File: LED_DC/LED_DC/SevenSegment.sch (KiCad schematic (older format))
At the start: 15 parts

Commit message: Removed redundant files
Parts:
- gave numbers to parts that had none: 15
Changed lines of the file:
@@
 $EndDescr
 $Comp
-L Display_Character:KCSA02-136 U?
+L Display_Character:KCSA02-136 U9
 U 1 1 5FB55AD1
 P 7650 2000
-F 0 "U?" H 7650 2667 50  0000 C CNN
+F 0 "U9" H 7650 2667 50  0000 C CNN
 F 1 "KCSA02-136" H 7650 2576 50  0000 C CNN
 F 2 "Display_7Segment:KCSC02-136" H 7650 1400 50  0001 C CNN
@@
 DP
 $Comp
-L Display_Character:KCSA02-136 U?
+L Display_Character:KCSA02-136 U3
 U 1 1 5FB5CA24
 P 1200 2000
-F 0 "U?" H 1200 2667 50  0000 C CNN
+F 0 "U3" H 1200 2667 50  0000 C CNN
 F 1 "KCSA02-136" H 1200 2576 50  0000 C CNN
 F 2 "Display_7Segment:KCSC02-136" H 1200 1400 50  0001 C CNN
@@
 DP
 $Comp
-L Display_Character:KCSA02-136 U?
+L Display_Character:KCSA02-136 U4
 U 1 1 5FB5E544
 P 2450 2000
-F 0 "U?" H 2450 2667 50  0000 C CNN
+F 0 "U4" H 2450 2667 50  0000 C CNN
 F 1 "KCSA02-136" H 2450 2576 50  0000 C CNN
 F 2 "Display_7Segment:KCSC02-136" H 2450 1400 50  0001 C CNN
@@
 DP
 $Comp
-L Display_Character:KCSA02-136 U?
+L Display_Character:KCSA02-136 U5
 U 1 1 5FB5F30B
 P 3550 2000
-F 0 "U?" H 3550 2667 50  0000 C CNN
+F 0 "U5" H 3550 2667 50  0000 C CNN
 F 1 "KCSA02-136" H 3550 2576 50  0000 C CNN
 F 2 "Display_7Segment:KCSC02-136" H 3550 1400 50  0001 C CNN
@@
 DP
 $Comp
-L Display_Character:KCSA02-136 U?
+L Display_Character:KCSA02-136 U6
 U 1 1 5FB6054A
 P 4550 2000
-F 0 "U?" H 4550 2667 50  0000 C CNN
+F 0 "U6" H 4550 2667 50  0000 C CNN
 F 1 "KCSA02-136" H 4550 2576 50  0000 C CNN
 F 2 "Display_7Segment:KCSC02-136" H 4550 1400 50  0001 C CNN
@@
 DP
 $Comp
-L Display_Character:KCSA02-136 U?
+L Display_Character:KCSA02-136 U7
 U 1 1 5FB633C5
 P 5550 2000
-F 0 "U?" H 5550 2667 50  0000 C CNN
+F 0 "U7" H 5550 2667 50  0000 C CNN
 F 1 "KCSA02-136" H 5550 2576 50  0000 C CNN
 F 2 "Display_7Segment:KCSC02-136" H 5550 1400 50  0001 C CNN
@@
 DP
 $Comp
-L Display_Character:KCSA02-136 U?
+L Display_Character:KCSA02-136 U8
 U 1 1 5FB65C47
 P 6550 2000
-F 0 "U?" H 6550 2667 50  0000 C CNN
+F 0 "U8" H 6550 2667 50  0000 C CNN
 F 1 "KCSA02-136" H 6550 2576 50  0000 C CNN
 F 2 "Display_7Segment:KCSC02-136" H 6550 1400 50  0001 C CNN
@@
 DP
 $Comp
-L Device:LED D?
+L Device:LED D2
 U 1 1 5FAF58A5
 P 4750 4800
-F 0 "D?" H 4743 5017 50  0000 C CNN
+F 0 "D2" H 4743 5017 50  0000 C CNN
 F 1 "LED" H 4743 4926 50  0000 C CNN
 F 2 "" H 4750 4800 50  0001 C CNN
@@
 $EndComp
 $Comp
-L Device:LED D?
+L Device:LED D5
 U 1 1 5FAF841D
 P 5850 4350
-F 0 "D?" H 5843 4567 50  0000 C CNN
+F 0 "D5" H 5843 4567 50  0000 C CNN
 F 1 "LED" H 5843 4476 50  0000 C CNN
 F 2 "" H 5850 4350 50  0001 C CNN
@@
 $EndComp
 $Comp
-L Device:LED D?
+L Device:LED D1
 U 1 1 5FAFB32B
 P 4750 4450
-F 0 "D?" H 4743 4667 50  0000 C CNN
+F 0 "D1" H 4743 4667 50  0000 C CNN
 F 1 "LED" H 4743 4576 50  0000 C CNN
 F 2 "" H 4750 4450 50  0001 C CNN
@@
 $EndComp
 $Comp
-L Device:LED D?
+L Device:LED D3
 U 1 1 5FAFBFC1
 P 4750 5150
-F 0 "D?" H 4743 5367 50  0000 C CNN
+F 0 "D3" H 4743 5367 50  0000 C CNN
 F 1 "LED" H 4743 5276 50  0000 C CNN
 F 2 "" H 4750 5150 50  0001 C CNN
@@
 $EndComp
 $Comp
-L Device:LED D?
+L Device:LED D4
 U 1 1 5FAFC42C
 P 4750 5500
-F 0 "D?" H 4743 5717 50  0000 C CNN
+F 0 "D4" H 4743 5717 50  0000 C CNN
 F 1 "LED" H 4743 5626 50  0000 C CNN
 F 2 "" H 4750 5500 50  0001 C CNN
@@
 $EndComp
 $Comp
-L Device:LED D?
+L Device:LED D6
 U 1 1 5FAFC938
 P 5850 4750
-F 0 "D?" H 5843 4967 50  0000 C CNN
+F 0 "D6" H 5843 4967 50  0000 C CNN
 F 1 "LED" H 5843 4876 50  0000 C CNN
 F 2 "" H 5850 4750 50  0001 C CNN
@@
 $EndComp
 $Comp
-L Device:LED D?
+L Device:LED D7
 U 1 1 5FAFCD00
 P 5850 5100
-F 0 "D?" H 5843 5317 50  0000 C CNN
+F 0 "D7" H 5843 5317 50  0000 C CNN
 F 1 "LED" H 5843 5226 50  0000 C CNN
 F 2 "" H 5850 5100 50  0001 C CNN
@@
 $EndComp
 $Comp
-L Device:LED D?
+L Device:LED D8
 U 1 1 5FAFD0BD
 P 5850 5500
-F 0 "D?" H 5843 5717 50  0000 C CNN
+F 0 "D8" H 5843 5717 50  0000 C CNN
 F 1 "LED" H 5843 5626 50  0000 C CNN
 F 2 "" H 5850 5500 50  0001 C CNN

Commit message: Added foot prints for the components.
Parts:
- D1, D2, D3, D4, D5, D6, D7, D8: footprint (none) -> LED_SMD:LED_0603_1608Metric_Pad1.05x0.95mm_HandSolder
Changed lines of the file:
@@
 F 0 "D2" H 4743 5017 50  0000 C CNN
 F 1 "LED" H 4743 4926 50  0000 C CNN
-F 2 "" H 4750 4800 50  0001 C CNN
+F 2 "LED_SMD:LED_0603_1608Metric_Pad1.05x0.95mm_HandSolder" H 4750 4800 50  0001 C CNN
 F 3 "~" H 4750 4800 50  0001 C CNN
 	1    4750 4800
@@
 F 0 "D5" H 5843 4567 50  0000 C CNN
 F 1 "LED" H 5843 4476 50  0000 C CNN
-F 2 "" H 5850 4350 50  0001 C CNN
+F 2 "LED_SMD:LED_0603_1608Metric_Pad1.05x0.95mm_HandSolder" H 5850 4350 50  0001 C CNN
 F 3 "~" H 5850 4350 50  0001 C CNN
 	1    5850 4350
@@
 F 0 "D1" H 4743 4667 50  0000 C CNN
 F 1 "LED" H 4743 4576 50  0000 C CNN
-F 2 "" H 4750 4450 50  0001 C CNN
+F 2 "LED_SMD:LED_0603_1608Metric_Pad1.05x0.95mm_HandSolder" H 4750 4450 50  0001 C CNN
 F 3 "~" H 4750 4450 50  0001 C CNN
 	1    4750 4450
@@
 F 0 "D3" H 4743 5367 50  0000 C CNN
 F 1 "LED" H 4743 5276 50  0000 C CNN
-F 2 "" H 4750 5150 50  0001 C CNN
+F 2 "LED_SMD:LED_0603_1608Metric_Pad1.05x0.95mm_HandSolder" H 4750 5150 50  0001 C CNN
 F 3 "~" H 4750 5150 50  0001 C CNN
 	1    4750 5150
@@
 F 0 "D4" H 4743 5717 50  0000 C CNN
 F 1 "LED" H 4743 5626 50  0000 C CNN
-F 2 "" H 4750 5500 50  0001 C CNN
+F 2 "LED_SMD:LED_0603_1608Metric_Pad1.05x0.95mm_HandSolder" H 4750 5500 50  0001 C CNN
 F 3 "~" H 4750 5500 50  0001 C CNN
 	1    4750 5500
@@
 F 0 "D6" H 5843 4967 50  0000 C CNN
 F 1 "LED" H 5843 4876 50  0000 C CNN
-F 2 "" H 5850 4750 50  0001 C CNN
+F 2 "LED_SMD:LED_0603_1608Metric_Pad1.05x0.95mm_HandSolder" H 5850 4750 50  0001 C CNN
 F 3 "~" H 5850 4750 50  0001 C CNN
 	1    5850 4750
@@
 F 0 "D7" H 5843 5317 50  0000 C CNN
 F 1 "LED" H 5843 5226 50  0000 C CNN
-F 2 "" H 5850 5100 50  0001 C CNN
+F 2 "LED_SMD:LED_0603_1608Metric_Pad1.05x0.95mm_HandSolder" H 5850 5100 50  0001 C CNN
 F 3 "~" H 5850 5100 50  0001 C CNN
 	1    5850 5100
@@
 F 0 "D8" H 5843 5717 50  0000 C CNN
 F 1 "LED" H 5843 5626 50  0000 C CNN
-F 2 "" H 5850 5500 50  0001 C CNN
+F 2 "LED_SMD:LED_0603_1608Metric_Pad1.05x0.95mm_HandSolder" H 5850 5500 50  0001 C CNN
 F 3 "~" H 5850 5500 50  0001 C CNN
 	1    5850 5500

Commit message: updated the foot print assignment.
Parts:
- U3, U4, U5, U6, U7, U8, U9: footprint Display_7Segment:KCSC02-136 -> Display_7Segment:7SegmentLED_LTS6760_LTS6780
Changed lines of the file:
@@
 F 0 "U9" H 7650 2667 50  0000 C CNN
 F 1 "KCSA02-136" H 7650 2576 50  0000 C CNN
-F 2 "Display_7Segment:KCSC02-136" H 7650 1400 50  0001 C CNN
+F 2 "Display_7Segment:7SegmentLED_LTS6760_LTS6780" H 7650 1400 50  0001 C CNN
 F 3 "http://www.kingbright.com/attachments/file/psearch/000/00/00/KCSA02-136(Ver.7B).pdf" H 7150 2475 50  0001 L CNN
 	1    7650 2000
@@
 F 0 "U3" H 1200 2667 50  0000 C CNN
 F 1 "KCSA02-136" H 1200 2576 50  0000 C CNN
-F 2 "Display_7Segment:KCSC02-136" H 1200 1400 50  0001 C CNN
+F 2 "Display_7Segment:7SegmentLED_LTS6760_LTS6780" H 1200 1400 50  0001 C CNN
 F 3 "http://www.kingbright.com/attachments/file/psearch/000/00/00/KCSA02-136(Ver.7B).pdf" H 700 2475 50  0001 L CNN
 	1    1200 2000
@@
 F 0 "U4" H 2450 2667 50  0000 C CNN
 F 1 "KCSA02-136" H 2450 2576 50  0000 C CNN
-F 2 "Display_7Segment:KCSC02-136" H 2450 1400 50  0001 C CNN
+F 2 "Display_7Segment:7SegmentLED_LTS6760_LTS6780" H 2450 1400 50  0001 C CNN
 F 3 "http://www.kingbright.com/attachments/file/psearch/000/00/00/KCSA02-136(Ver.7B).pdf" H 1950 2475 50  0001 L CNN
 	1    2450 2000
@@
 F 0 "U5" H 3550 2667 50  0000 C CNN
 F 1 "KCSA02-136" H 3550 2576 50  0000 C CNN
-F 2 "Display_7Segment:KCSC02-136" H 3550 1400 50  0001 C CNN
+F 2 "Display_7Segment:7SegmentLED_LTS6760_LTS6780" H 3550 1400 50  0001 C CNN
 F 3 "http://www.kingbright.com/attachments/file/psearch/000/00/00/KCSA02-136(Ver.7B).pdf" H 3050 2475 50  0001 L CNN
 	1    3550 2000
@@
 F 0 "U6" H 4550 2667 50  0000 C CNN
 F 1 "KCSA02-136" H 4550 2576 50  0000 C CNN
-F 2 "Display_7Segment:KCSC02-136" H 4550 1400 50  0001 C CNN
+F 2 "Display_7Segment:7SegmentLED_LTS6760_LTS6780" H 4550 1400 50  0001 C CNN
 F 3 "http://www.kingbright.com/attachments/file/psearch/000/00/00/KCSA02-136(Ver.7B).pdf" H 4050 2475 50  0001 L CNN
 	1    4550 2000
@@
 F 0 "U7" H 5550 2667 50  0000 C CNN
 F 1 "KCSA02-136" H 5550 2576 50  0000 C CNN
-F 2 "Display_7Segment:KCSC02-136" H 5550 1400 50  0001 C CNN
+F 2 "Display_7Segment:7SegmentLED_LTS6760_LTS6780" H 5550 1400 50  0001 C CNN
 F 3 "http://www.kingbright.com/attachments/file/psearch/000/00/00/KCSA02-136(Ver.7B).pdf" H 5050 2475 50  0001 L CNN
 	1    5550 2000
@@
 F 0 "U8" H 6550 2667 50  0000 C CNN
 F 1 "KCSA02-136" H 6550 2576 50  0000 C CNN
-F 2 "Display_7Segment:KCSC02-136" H 6550 1400 50  0001 C CNN
+F 2 "Display_7Segment:7SegmentLED_LTS6760_LTS6780" H 6550 1400 50  0001 C CNN
 F 3 "http://www.kingbright.com/attachments/file/psearch/000/00/00/KCSA02-136(Ver.7B).pdf" H 6050 2475 50  0001 L CNN
 	1    6550 2000

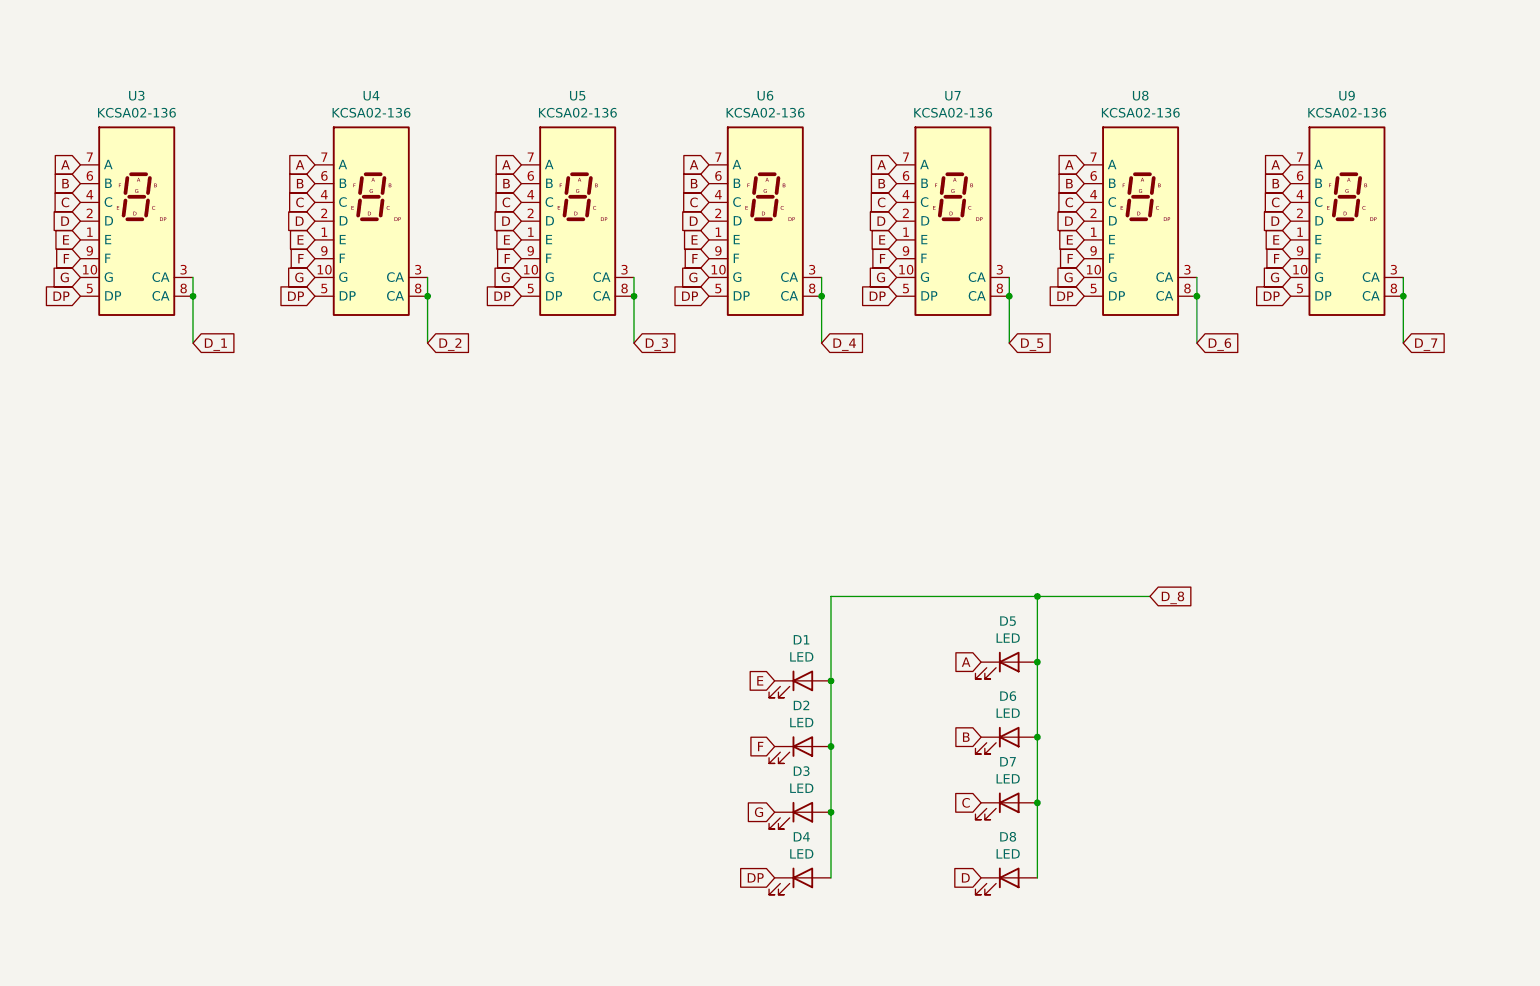
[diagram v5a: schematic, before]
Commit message: Added text to the schematic sections.
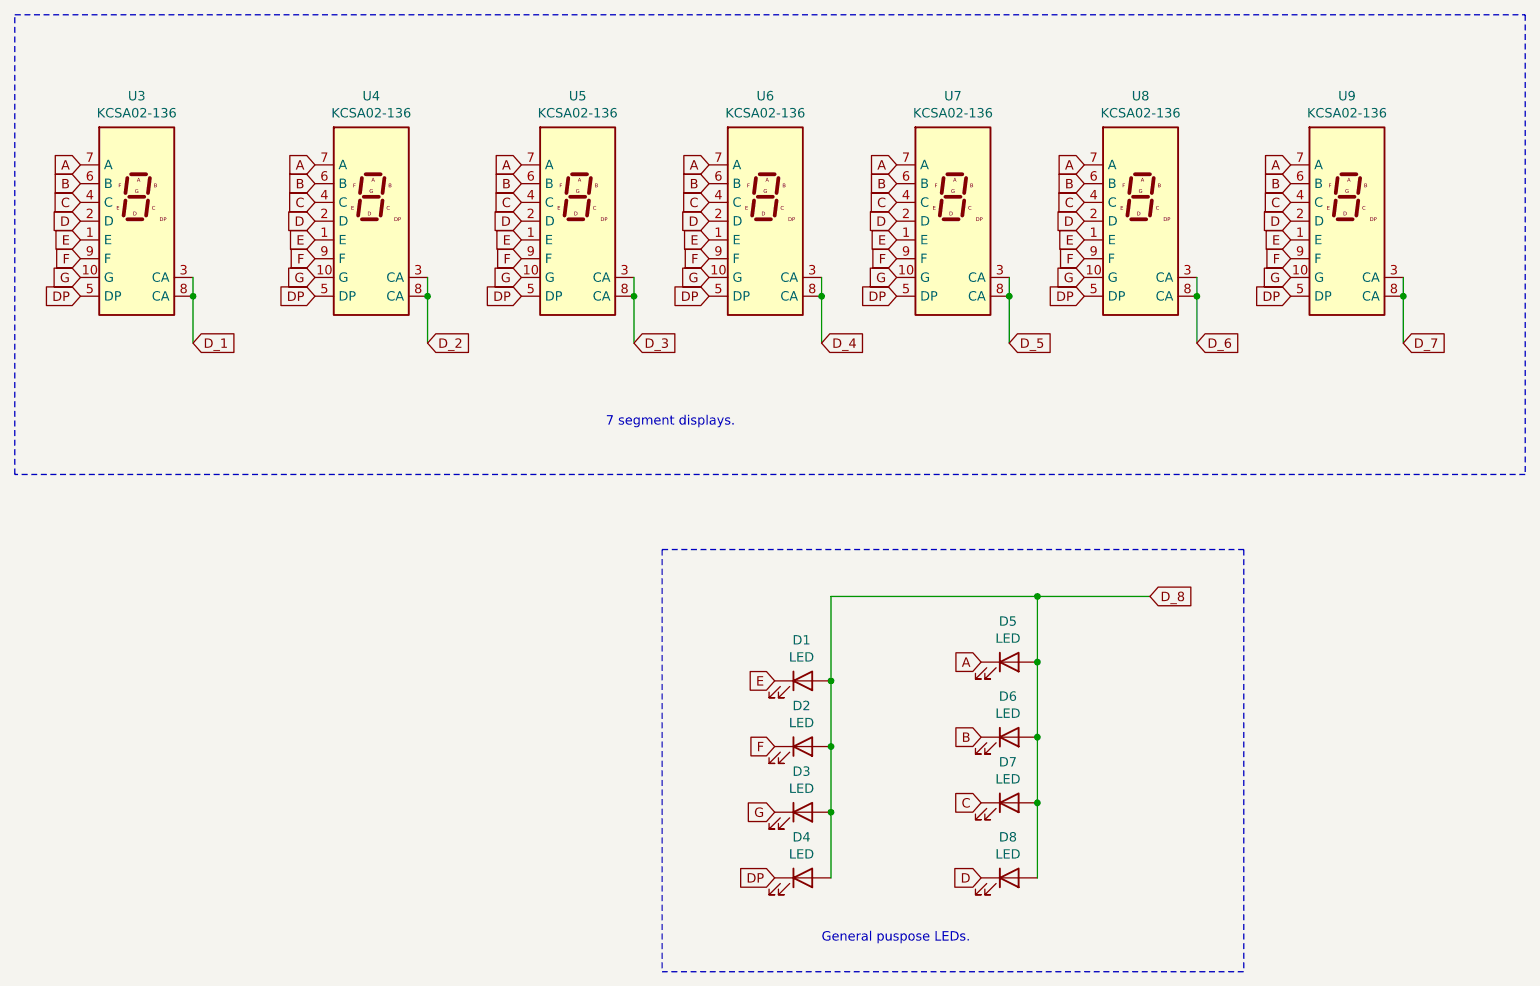
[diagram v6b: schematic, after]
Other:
- note added: "7 segment displays."
- note added: "General puspose LEDs.\n"
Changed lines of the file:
@@
 Connection ~ 4900 4450
 Connection ~ 6000 4000
+Wire Notes Line
+	8600 900  8600 3350
+Wire Notes Line
+	8600 3350 550  3350
+Wire Notes Line
+	550  3350 550  900
+Wire Notes Line
+	550  900  8600 900
+Text Notes 3700 3100 0    50   ~ 0
+7 segment displays.
+Wire Notes Line
+	7100 3750 7100 6000
+Wire Notes Line
+	7100 6000 4000 6000
+Wire Notes Line
+	4000 3750 7100 3750
+Wire Notes Line
+	4000 3750 4000 6000
+Text Notes 4850 5850 0    50   ~ 0
+General puspose LEDs.\n
 $EndSCHEMATC

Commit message: Updated PCB.
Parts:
- D1, D2, D3, D4, D5, D6, D7, D8: footprint LED_SMD:LED_0603_1608Metric_Pad1.05x0.95mm_HandSolder -> LED_THT:LED_D3.0mm
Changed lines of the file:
@@
 F 0 "D2" H 4743 5017 50  0000 C CNN
 F 1 "LED" H 4743 4926 50  0000 C CNN
-F 2 "LED_SMD:LED_0603_1608Metric_Pad1.05x0.95mm_HandSolder" H 4750 4800 50  0001 C CNN
+F 2 "LED_THT:LED_D3.0mm" H 4750 4800 50  0001 C CNN
 F 3 "~" H 4750 4800 50  0001 C CNN
 	1    4750 4800
@@
 F 0 "D5" H 5843 4567 50  0000 C CNN
 F 1 "LED" H 5843 4476 50  0000 C CNN
-F 2 "LED_SMD:LED_0603_1608Metric_Pad1.05x0.95mm_HandSolder" H 5850 4350 50  0001 C CNN
+F 2 "LED_THT:LED_D3.0mm" H 5850 4350 50  0001 C CNN
 F 3 "~" H 5850 4350 50  0001 C CNN
 	1    5850 4350
@@
 F 0 "D1" H 4743 4667 50  0000 C CNN
 F 1 "LED" H 4743 4576 50  0000 C CNN
-F 2 "LED_SMD:LED_0603_1608Metric_Pad1.05x0.95mm_HandSolder" H 4750 4450 50  0001 C CNN
+F 2 "LED_THT:LED_D3.0mm" H 4750 4450 50  0001 C CNN
 F 3 "~" H 4750 4450 50  0001 C CNN
 	1    4750 4450
@@
 F 0 "D3" H 4743 5367 50  0000 C CNN
 F 1 "LED" H 4743 5276 50  0000 C CNN
-F 2 "LED_SMD:LED_0603_1608Metric_Pad1.05x0.95mm_HandSolder" H 4750 5150 50  0001 C CNN
+F 2 "LED_THT:LED_D3.0mm" H 4750 5150 50  0001 C CNN
 F 3 "~" H 4750 5150 50  0001 C CNN
 	1    4750 5150
@@
 F 0 "D4" H 4743 5717 50  0000 C CNN
 F 1 "LED" H 4743 5626 50  0000 C CNN
-F 2 "LED_SMD:LED_0603_1608Metric_Pad1.05x0.95mm_HandSolder" H 4750 5500 50  0001 C CNN
+F 2 "LED_THT:LED_D3.0mm" H 4750 5500 50  0001 C CNN
 F 3 "~" H 4750 5500 50  0001 C CNN
 	1    4750 5500
@@
 F 0 "D6" H 5843 4967 50  0000 C CNN
 F 1 "LED" H 5843 4876 50  0000 C CNN
-F 2 "LED_SMD:LED_0603_1608Metric_Pad1.05x0.95mm_HandSolder" H 5850 4750 50  0001 C CNN
+F 2 "LED_THT:LED_D3.0mm" H 5850 4750 50  0001 C CNN
 F 3 "~" H 5850 4750 50  0001 C CNN
 	1    5850 4750
@@
 F 0 "D7" H 5843 5317 50  0000 C CNN
 F 1 "LED" H 5843 5226 50  0000 C CNN
-F 2 "LED_SMD:LED_0603_1608Metric_Pad1.05x0.95mm_HandSolder" H 5850 5100 50  0001 C CNN
+F 2 "LED_THT:LED_D3.0mm" H 5850 5100 50  0001 C CNN
 F 3 "~" H 5850 5100 50  0001 C CNN
 	1    5850 5100
@@
 F 0 "D8" H 5843 5717 50  0000 C CNN
 F 1 "LED" H 5843 5626 50  0000 C CNN
-F 2 "LED_SMD:LED_0603_1608Metric_Pad1.05x0.95mm_HandSolder" H 5850 5500 50  0001 C CNN
+F 2 "LED_THT:LED_D3.0mm" H 5850 5500 50  0001 C CNN
 F 3 "~" H 5850 5500 50  0001 C CNN
 	1    5850 5500

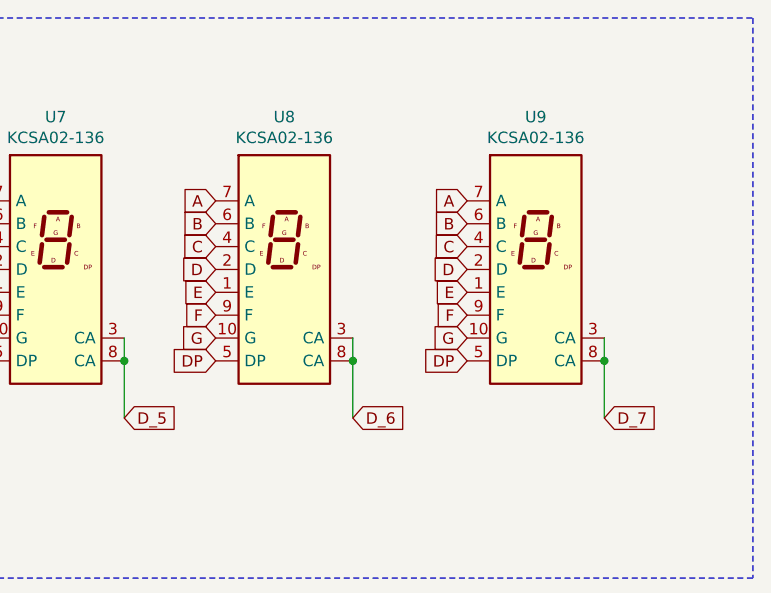
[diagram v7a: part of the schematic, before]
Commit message: Updated the LED DC PCB.
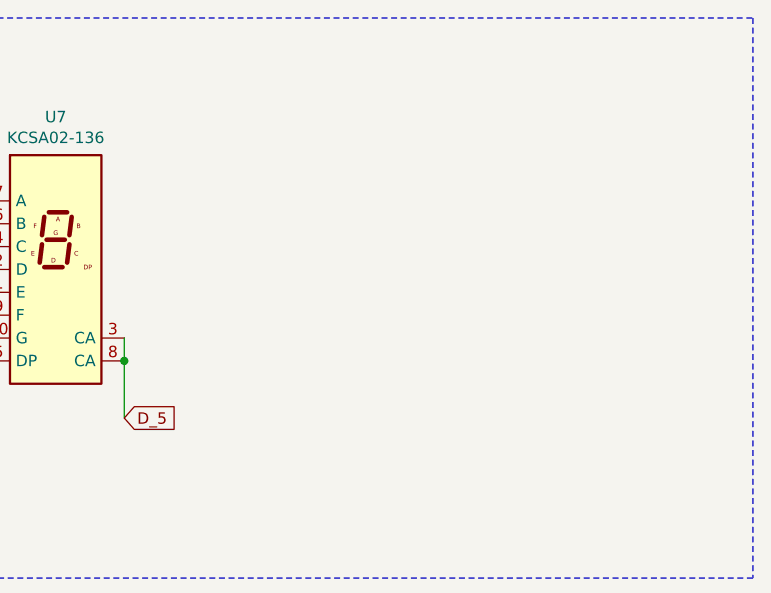
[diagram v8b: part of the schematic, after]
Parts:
- removed U8, U9: KCSA02-136, Display_7Segment:7SegmentLED_LTS6760_LTS6780, symbol Display_Character:KCSA02-136
